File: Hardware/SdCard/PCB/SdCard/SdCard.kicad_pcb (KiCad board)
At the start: 2 copper layers, 38.1 x 33 mm, 7 parts, among them J1 Conn_01x08_Male, J2 Conn_01x08_Male

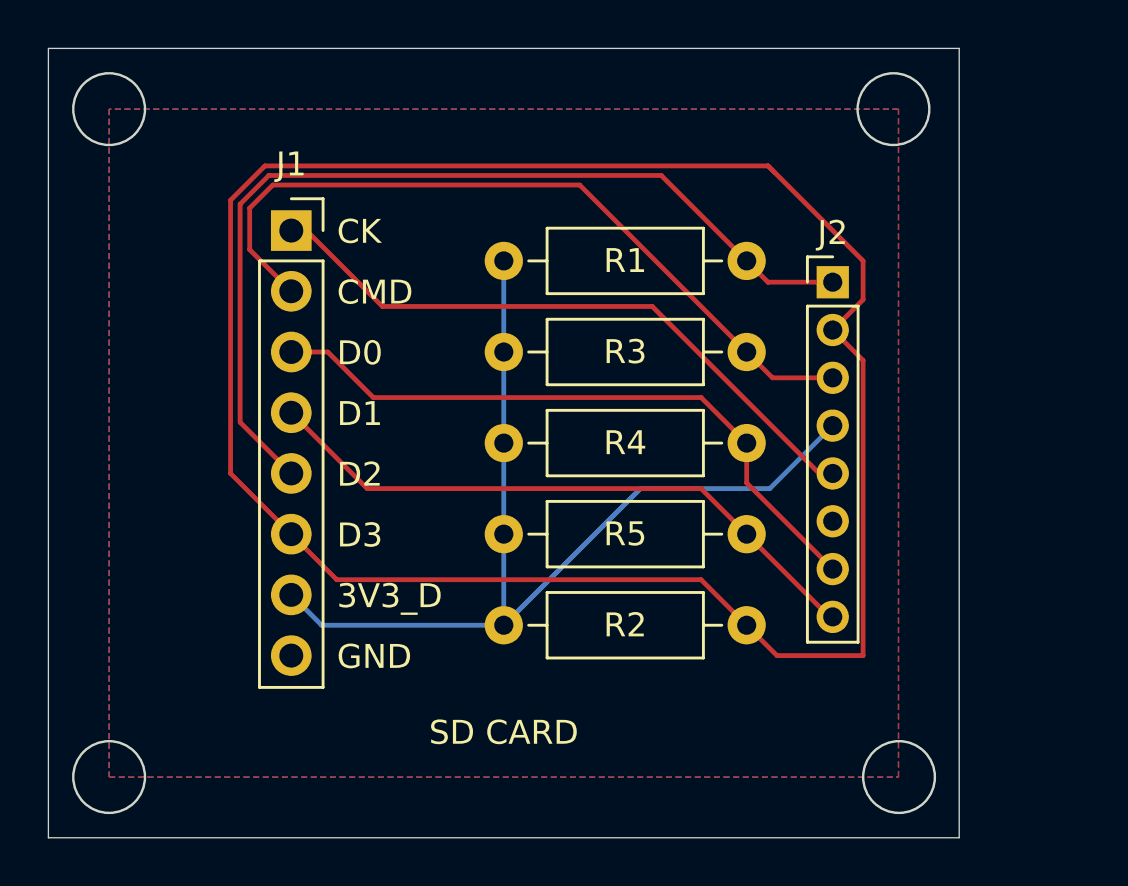
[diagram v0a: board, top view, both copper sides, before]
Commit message: Edges removed
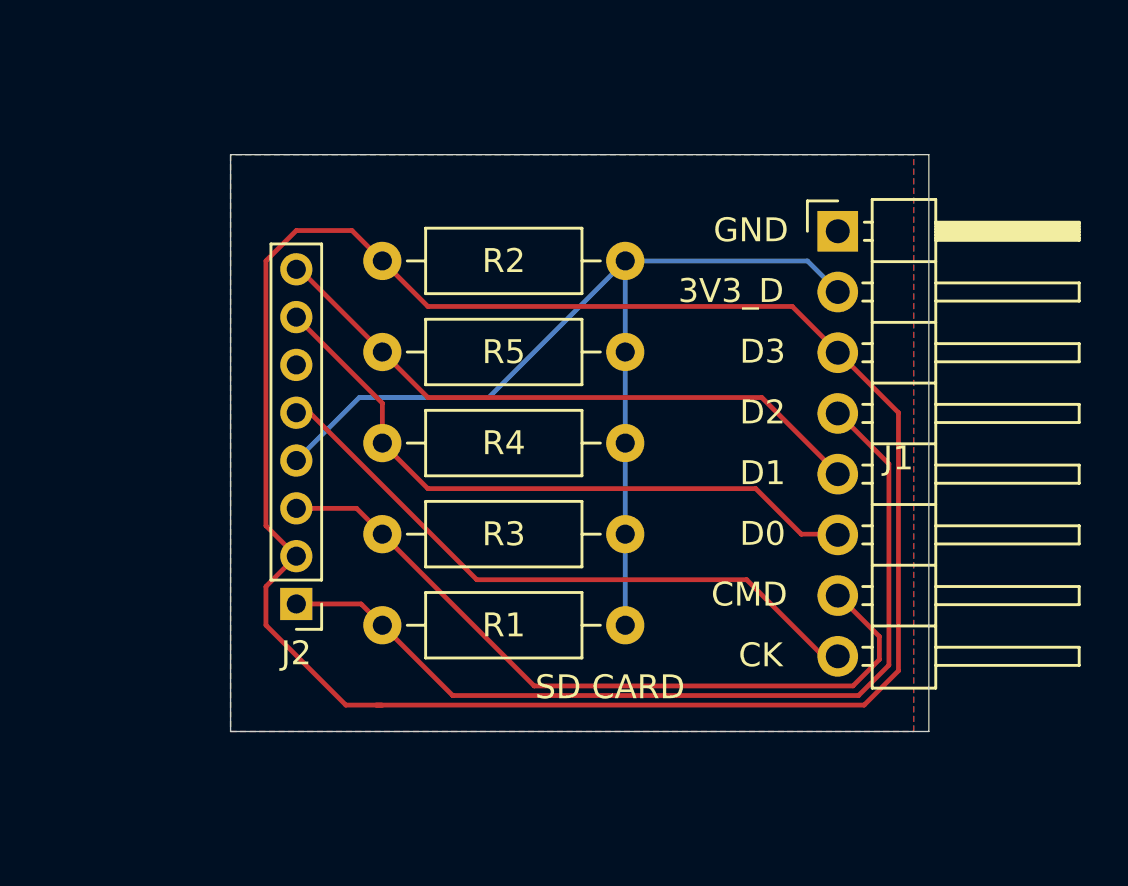
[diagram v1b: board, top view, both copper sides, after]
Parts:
- J1: footprint Connector_PinSocket_2.54mm:PinSocket_1x08_P2.54mm_Vertical -> Connector_PinHeader_2.54mm:PinHeader_1x08_P2.54mm_Horizontal
- moved J2 26.2 mm to (101.8, 89.3), turned to 180 degrees
- moved J1 22.9 mm to (124.5, 73.7)
- moved R1 21.6 mm to (105.4, 90.2), turned to 0 degrees
- moved R2 21.6 mm to (105.4, 74.9), turned to 0 degrees
- moved R3 17.0 mm to (105.4, 86.4), turned to 0 degrees
- moved R5 17.0 mm to (105.4, 78.7), turned to 0 degrees
- moved R4 15.2 mm to (105.4, 82.5), turned to 0 degrees
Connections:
- J1 pad 1: SDMMC1_CK -> GND
- J1 pad 2: SDMMC1_CMD -> 3V3_D
- J1 pad 3: SDMMC1_D0 -> SDMMC1_D3
- J1 pad 4: SDMMC1_D1 -> SDMMC1_D2
- J1 pad 5: SDMMC1_D2 -> SDMMC1_D1
- J1 pad 6: SDMMC1_D3 -> SDMMC1_D0
- J1 pad 7: 3V3_D -> SDMMC1_CMD
- J1 pad 8: GND -> SDMMC1_CK
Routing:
- net SDMMC1_D3: track 87.7 -> 85.9 mm
- net SDMMC1_CMD: track 33.0 -> 32.0 mm
- net SDMMC1_D2: track 39.3 -> 38.3 mm
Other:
- board size 38.1 x 33 mm -> 29.2 x 24.1 mm
